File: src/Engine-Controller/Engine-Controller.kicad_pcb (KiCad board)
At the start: 4 copper layers, 109.2 x 56.7 mm, 127 parts, among them J2 Jumper_NO, P1 EJ508A, P16 647676-2, P17 0530470410, P18 PPTC041LFBN-RC, P2 282837-6, P3 3220-20-0200-00, P4 Micro_SD_Card, P5 USB, P6 140-504-415-000, P7 647676-2, P8 20021511-00026T4LF, P9 5015680807, Q1 QS5U17TR, U1 STM32H750VBTx, U10 LMS8117AMP-3.3_NOPB, U11 TS391IYLT, U12 MAX4617EUE+T, U13 MAX4617EUE+T, U14 MCP96L01T-E_MX, U15 AD623ARZ-R7, U2 LM22672MRE-5.0_NOPB, U3 LMS8117AMP-3.3_NOPB, U4 SST25VF040B-50-4I-S2AE-T, U5 CP2102-GMR(QFN28), U6 TPS2115APWR, U7 MC74HC4066ADG, U8 AD623ARZ-R7, U9 MC74HC4066ADG, Y1 ECS-240-18-33-JGN-TR

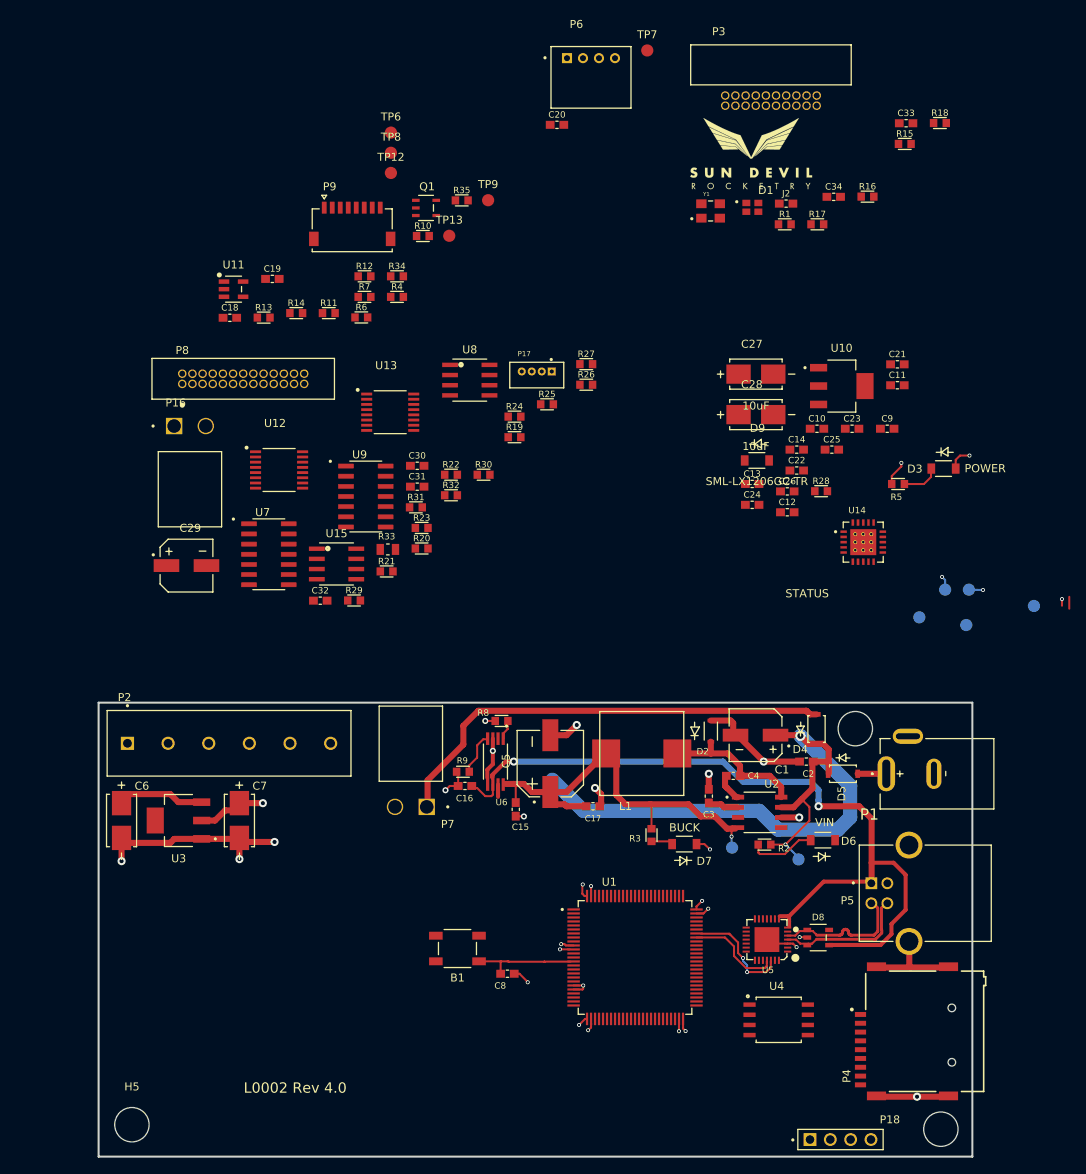
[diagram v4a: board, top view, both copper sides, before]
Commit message: added safety switch to schematic
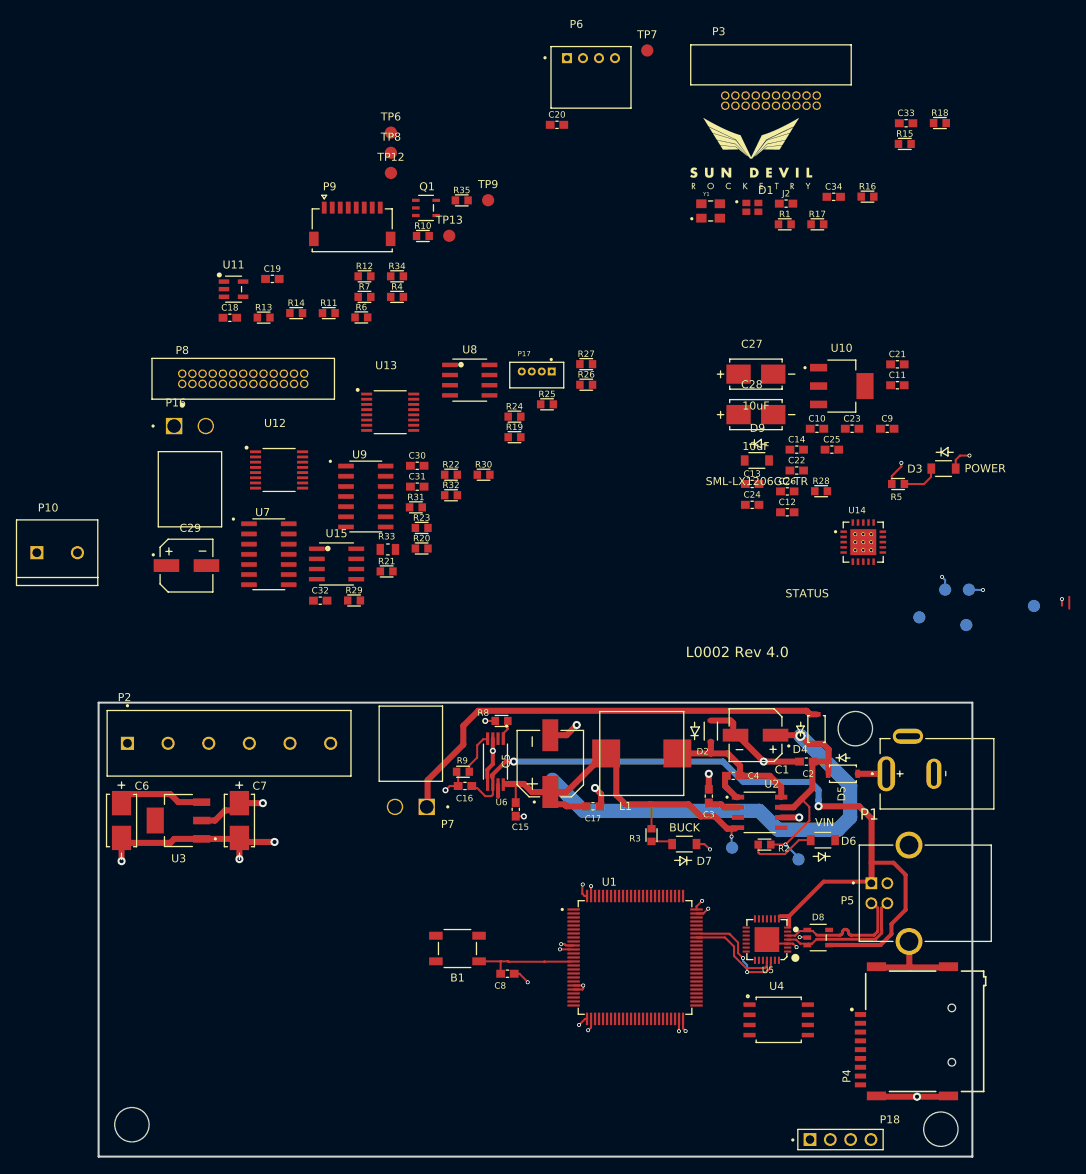
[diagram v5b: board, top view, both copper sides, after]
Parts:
- added P10: 282837-2, Engine-Controller:282837-2, F.Cu at (88.8, 76.9)
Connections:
- P2 pad 1: VIN -> Net-(P2-Pad1)
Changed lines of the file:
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@@
   (net 28 "Net-(D9-Pad1)")
   (net 29 "BOOT")
-  (net 30 "Net-(P2-Pad2)")
+  (net 30 "Net-(P2-Pad1)")
   (net 31 "unconnected-(P3-Pad11)")
   (net 32 "unconnected-(P3-Pad17)")
@@
   (net 174 "unconnected-(U14-Pad15)")
   (net 175 "unconnected-(U1-Pad34)")
+  (net 176 "Net-(Q1-Pad5)")
   (footprint "Engine-Controller:CWR11HH106KB" (layer "F.Cu")
     (at 96.8502 110.3884 -90)
@@
     (fp_line (start -0.9 -0.5) (end 0.9 -0.5) (layer "F.Fab") (width 0.127))
     (pad "1" smd rect (at -0.79 0) (size 0.94 1.02) (layers "F.Cu" "F.Paste" "F.Mask")
-      (net 30 "Net-(P2-Pad2)") (pintype "passive"))
+      (net 176 "Net-(Q1-Pad5)") (pintype "passive"))
     (pad "2" smd rect (at 0.79 0) (size 0.94 1.02) (layers "F.Cu" "F.Paste" "F.Mask")
       (net 1 "Earth") (pintype "passive"))
@@
     (pad "4" smd rect (at 1.27635 0.950001) (size 0.9525 0.4064) (layers "F.Cu" "F.Paste" "F.Mask"))
     (pad "5" smd rect (at 1.27635 -0.950001) (size 0.9525 0.4064) (layers "F.Cu" "F.Paste" "F.Mask")
-      (net 30 "Net-(P2-Pad2)") (pinfunction "D") (pintype "passive"))
+      (net 176 "Net-(Q1-Pad5)") (pinfunction "D") (pintype "passive"))
     (model "/home/olsport/Documents/SDR/PCB/Liquids-Engine-Controller/CAD/3Dfiles/TRANS_QS5K_ROM.step"
       (offset (xyz 0 0 0))
@@
     (property "Sheetname" "")
     (attr exclude_from_pos_files)
-    (fp_text reference "H5" (at 0 -4.75) (layer "F.SilkS")
+    (fp_text reference "H5" (at 0 -4.75) (layer "F.SilkS") hide
       (effects (font (size 1 1) (thickness 0.15)))
     )
-    (fp_text value "Mounting-Hole" (at 0 4.75) (layer "F.Fab")
+    (fp_text value "Mounting-Hole" (at 0 4.75) (layer "F.Fab") hide
       (effects (font (size 1 1) (thickness 0.15)))
     )
-    (fp_text user "${REFERENCE}" (at 0.3 0) (layer "F.Fab")
+    (fp_text user "${REFERENCE}" (at 0.3 0) (layer "F.Fab") hide
       (effects (font (size 1 1) (thickness 0.15)))
     )
@@
     (fp_circle (center -12.7 -4.7) (end -12.6 -4.7) (layer "F.Fab") (width 0.2) (fill none))
     (pad "1" thru_hole rect (at -12.7 0) (size 1.65 1.65) (drill 1.1) (layers *.Cu *.Mask)
-      (net 100 "VIN") (pinfunction "5") (pintype "passive"))
+      (net 30 "Net-(P2-Pad1)") (pinfunction "5") (pintype "passive"))
     (pad "2" thru_hole circle (at -7.62 0) (size 1.65 1.65) (drill 1.1) (layers *.Cu *.Mask)
-      (net 30 "Net-(P2-Pad2)") (pinfunction "6") (pintype "passive"))
+      (net 176 "Net-(Q1-Pad5)") (pinfunction "6") (pintype "passive"))
     (pad "3" thru_hole circle (at -2.54 0) (size 1.65 1.65) (drill 1.1) (layers *.Cu *.Mask)
       (net 119 "SP_CONT") (pinfunction "5") (pintype "passive"))
@@
       (net 11 "5V") (pinfunction "-") (pintype "input"))
     (pad "4" smd rect (at 1.1938 0.950001) (size 1.3208 0.5588) (layers "F.Cu" "F.Paste" "F.Mask")
-      (net 30 "Net-(P2-Pad2)") (pinfunction "+") (pintype "input"))
+      (net 176 "Net-(Q1-Pad5)") (pinfunction "+") (pintype "input"))
     (pad "5" smd rect (at 1.1938 -0.950001) (size 1.3208 0.5588) (layers "F.Cu" "F.Paste" "F.Mask")
       (net 100 "VIN") (pinfunction "V+") (pintype "passive"))
@@
     )
   )
+  (footprint "Engine-Controller:282837-2" (layer "F.Cu")
+    (at 88.7984 76.9112)
+    (property "Field2" "Ignition")
+    (property "Field3" "USB")
+    (property "Field4" "Flash")
+    (property "Field5" "SD Card")
+    (property "Field6" "Valve Controller")
+    (property "Field7" "Wireless Interface")
+    (property "Sheetfile" "Page2.kicad_sch")
+    (property "Sheetname" "Page2")
+    (attr through_hole)
+    (fp_text reference "P10" (at -1.127255 -5.614945) (layer "F.SilkS")
+      (effects (font (size 1.002039 1.002039) (thickness 0.15)))
+    )
+    (fp_text value "282837-2" (at 2.69202 5.84743) (layer "F.Fab")
+      (effects (font (size 1.002614 1.002614) (thickness 0.15)))
+    )
+    (fp_line (start -5.08 -4.1) (end 5.08 -4.1) (layer "F.SilkS") (width 0.127))
+    (fp_line (start -5.08 3.1) (end -5.08 -4.1) (layer "F.SilkS") (width 0.127))
+    (fp_line (start 5.08 -4.1) (end 5.08 3.1) (layer "F.SilkS") (width 0.127))
+    (fp_line (start 5.08 4.1) (end -5.08 4.1) (layer "F.SilkS") (width 0.127))
+    (fp_line (start -5.08 3.1) (end 5.08 3.1) (layer "F.SilkS") (width 0.127))
+    (fp_line (start -5.08 4.1) (end -5.08 3.1) (layer "F.SilkS") (width 0.127))
+    (fp_line (start 5.08 3.1) (end 5.08 4.1) (layer "F.SilkS") (width 0.127))
+    (fp_line (start -5.33 4.35) (end -5.33 -4.35) (layer "F.CrtYd") (width 0.05))
+    (fp_line (start 5.33 -4.35) (end 5.33 4.35) (layer "F.CrtYd") (width 0.05))
+    (fp_line (start 5.33 4.35) (end -5.33 4.35) (layer "F.CrtYd") (width 0.05))
+    (fp_line (start -5.33 -4.35) (end 5.33 -4.35) (layer "F.CrtYd") (width 0.05))
+    (fp_line (start 5.08 4.1) (end -5.08 4.1) (layer "F.Fab") (width 0.127))
+    (fp_line (start -5.08 -4.1) (end 5.08 -4.1) (layer "F.Fab") (width 0.127))
+    (fp_line (start 5.08 -4.1) (end 5.08 4.1) (layer "F.Fab") (width 0.127))
+    (fp_line (start -5.08 4.1) (end -5.08 -4.1) (layer "F.Fab") (width 0.127))
+    (fp_circle (center -2.54 1.27) (end -2.44 1.27) (layer "F.Fab") (width 0.2) (fill none))
+    (pad "1" thru_hole rect (at -2.54 0) (size 1.65 1.65) (drill 1.1) (layers *.Cu *.Mask)
+      (net 100 "VIN") (pinfunction "5") (pintype "passive"))
+    (pad "2" thru_hole circle (at 2.54 0) (size 1.65 1.65) (drill 1.1) (layers *.Cu *.Mask)
+      (net 30 "Net-(P2-Pad1)") (pinfunction "6") (pintype "passive"))
+    (model "/home/olsport/Documents/SDR/PCB/L0002-Liquids-Engine-Controller/CAD/3Dfiles/282837-2.step"
+      (offset (xyz 0 -4 2.5))
+      (scale (xyz 1 1 1))
+      (rotate (xyz -90 0 0))
+    )
+  )
   (footprint "Engine-Controller:RES_0603" (layer "F.Cu")
     (at 126.824 47.5038)
@@
     (effects (font (size 1.016 1.016) (thickness 0.2032)))
   )
-  (gr_text "L0002 Rev 4.0" (at 118.5545 143.8148) (layer "F.SilkS")
+  (gr_text "L0002 Rev 4.0" (at 173.8122 89.3572) (layer "F.SilkS")
     (effects (font (size 1.3 1.3) (thickness 0.2)))
   )

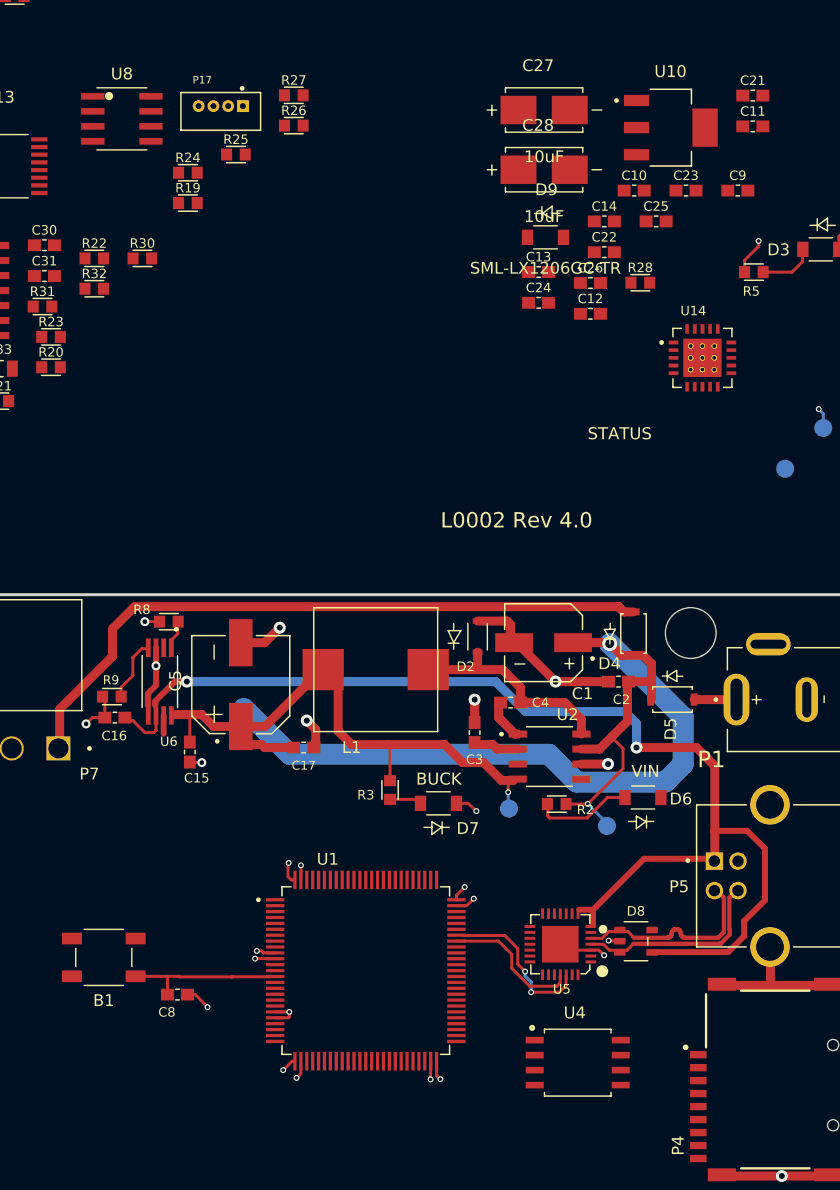
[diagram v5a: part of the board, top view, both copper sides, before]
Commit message: removed uncessary caps from MCU LDO pins
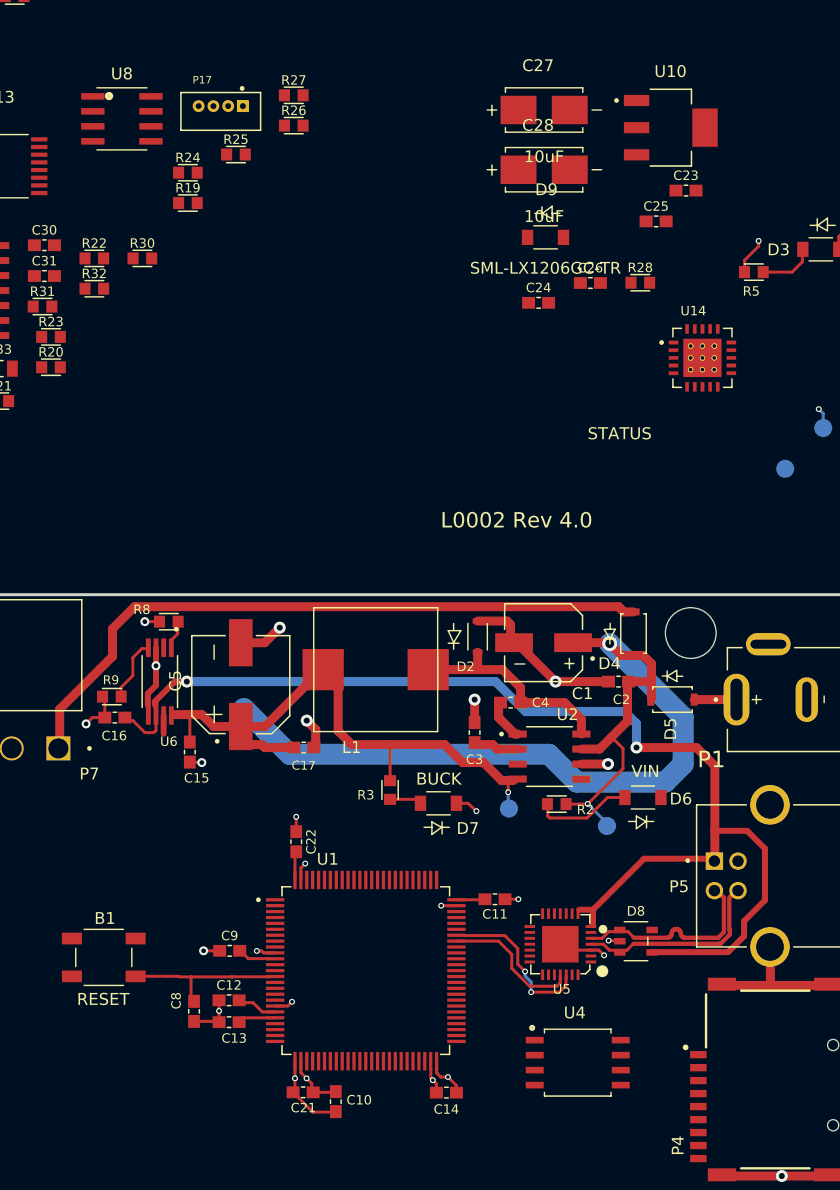
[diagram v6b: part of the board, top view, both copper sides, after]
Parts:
- moved C21 92.6 mm to (155.7, 137.8)
- moved C10 81.2 mm to (158.5, 138.6), turned to 90 degrees
- moved C9 77.5 mm to (149.5, 125.8)
- moved C14 75.0 mm to (167.9, 137.8)
- moved C11 69.0 mm to (172.0, 121.5), turned to 180 degrees
- moved C13 68.8 mm to (149.5, 131.9)
- moved C12 65.7 mm to (149.5, 130.0)
- moved C22 56.4 mm to (155.1, 116.6), turned to -90 degrees
- moved C8 1.99 mm to (146.5, 131.0), turned to 90 degrees
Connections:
- C11 pad 1: Earth -> Net-(C11-Pad1)
- C12 pad 2: 3.3V -> A3.3V
- C13 pad 2: 3.3V -> A3.3V
- C21 pad 1: Earth -> Net-(C11-Pad1)
- C9 pad 1: Earth -> Net-(C11-Pad1)
- U1 pad 59: unconnected-(U1-Pad59) -> FLASH_WP
- U1 pad 98: FLASH_WP -> unconnected-(U1-Pad98)
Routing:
- net Earth: track 100.3 -> 110.3 mm, vias 23 -> 25
- net 3.3V: track 21.0 -> 28.5 mm, vias 9 -> 6
- net A3.3V: track 2.85 -> 6.11 mm, vias 1 -> 0
- net Net-(C11-Pad1): track 0.00 -> 2.49 mm, vias 0 -> 2
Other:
- board text added: "RESET"
